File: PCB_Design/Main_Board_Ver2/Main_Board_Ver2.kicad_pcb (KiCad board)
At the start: 2 copper layers, 112.8 x 67.4 mm, 10 parts, among them J1 PJ-037A, J2 796949-4, J3 796949-4

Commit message: Making Changes to MAC variant
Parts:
- moved C5 0.14 mm to (188.2, 127.1)
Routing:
- net 12V: track 260.1 -> 186.9 mm
- net GND_Barrel: track 232.8 -> 171.8 mm, vias 2 -> 0
- net Uno_5V: track 70.6 -> 38.6 mm
- net GND_Uno: track 49.8 -> 24.0 mm
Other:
- net class Default removed

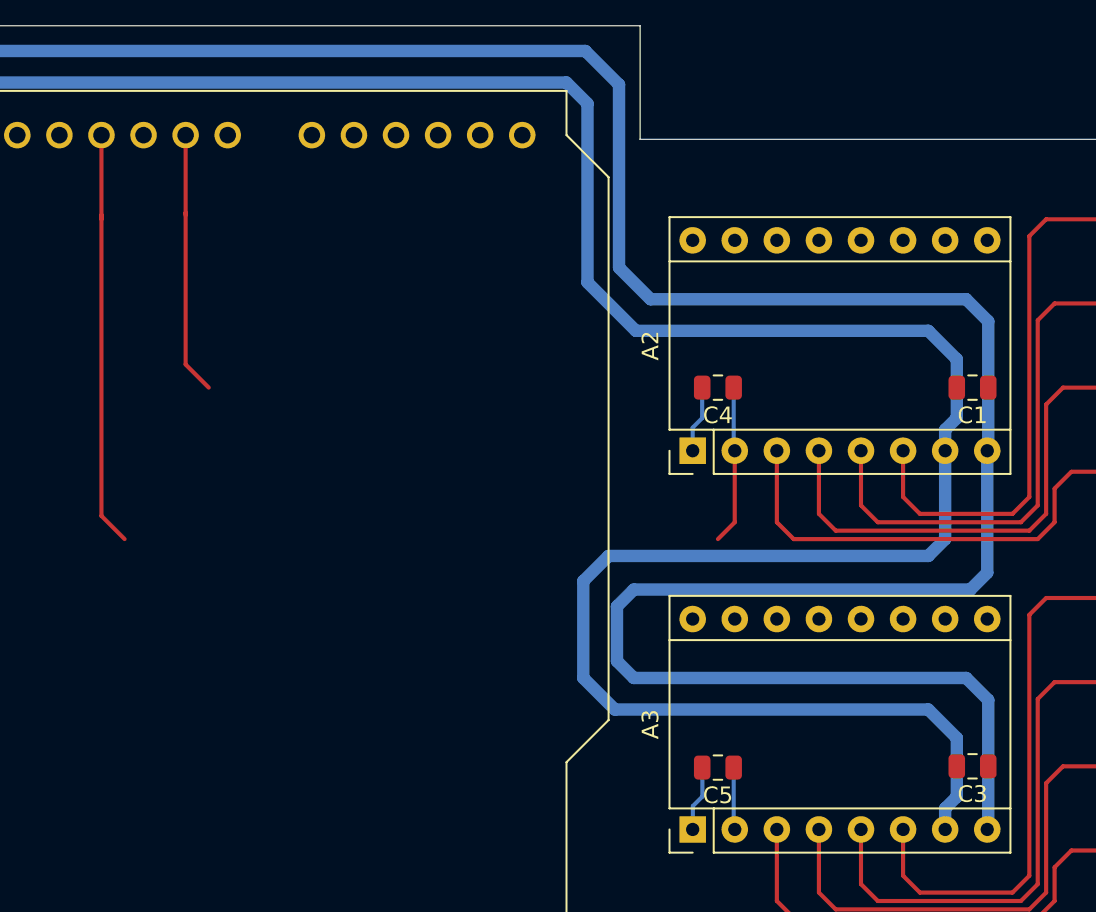
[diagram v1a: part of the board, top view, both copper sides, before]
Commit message: Finishing Power Lines
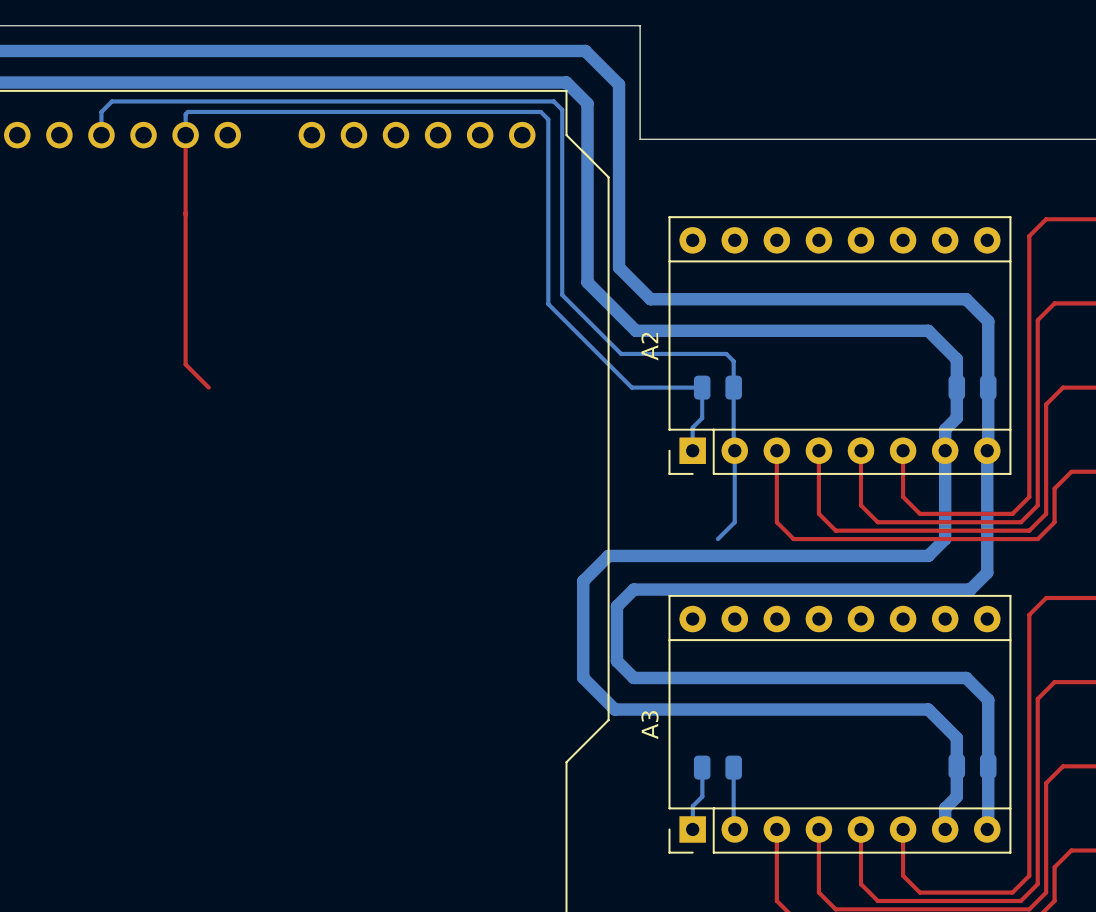
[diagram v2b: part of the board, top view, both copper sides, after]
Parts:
- C1, C3, C4, C5: moved to B.Cu
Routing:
- net GND_Uno: track 24.0 -> 70.0 mm
- net Uno_5V: track 38.6 -> 67.8 mm

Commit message: PCB Final
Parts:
- added REF**: MountingHole_3.2mm_M3_DIN965_Pad, MountingHole:MountingHole_3.2mm_M3_DIN965_Pad, F.Cu at (119.2, 68.5)
- added REF**: MountingHole_3.2mm_M3_DIN965_Pad, MountingHole:MountingHole_3.2mm_M3_DIN965_Pad, F.Cu at (119.2, 145.0)
- added REF**: MountingHole_3.2mm_M3_DIN965_Pad, MountingHole:MountingHole_3.2mm_M3_DIN965_Pad, F.Cu at (218.5, 141.0)
- added REF**: MountingHole_3.2mm_M3_DIN965_Pad, MountingHole:MountingHole_3.2mm_M3_DIN965_Pad, F.Cu at (218.5, 85.2)
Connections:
- A1 pad 1: Net-(A1-Pad1) -> unconnected-(A1-Pad1)
- A1 pad 10: Net-(A1-Pad10) -> unconnected-(A1-Pad10)
- A1 pad 11: Net-(A1-Pad11) -> unconnected-(A1-Pad11)
- A1 pad 12: Net-(A1-Pad12) -> unconnected-(A1-Pad12)
- A1 pad 13: Net-(A1-Pad13) -> unconnected-(A1-Pad13)
- A1 pad 14: Net-(A1-Pad14) -> unconnected-(A1-Pad14)
- A1 pad 15: Net-(A1-Pad15) -> unconnected-(A1-Pad15)
- A1 pad 16: Net-(A1-Pad16) -> unconnected-(A1-Pad16)
- A1 pad 2: Net-(A1-Pad2) -> unconnected-(A1-Pad2)
- A1 pad 21: Net-(A1-Pad21) -> unconnected-(A1-Pad21)
- A1 pad 22: Net-(A1-Pad22) -> unconnected-(A1-Pad22)
- A1 pad 23: Net-(A1-Pad23) -> unconnected-(A1-Pad23)
- A1 pad 24: Net-(A1-Pad24) -> unconnected-(A1-Pad24)
- A1 pad 25: Net-(A1-Pad25) -> unconnected-(A1-Pad25)
- A1 pad 26: Net-(A1-Pad26) -> unconnected-(A1-Pad26)
- A1 pad 27: Net-(A1-Pad27) -> unconnected-(A1-Pad27)
- A1 pad 28: Net-(A1-Pad28) -> unconnected-(A1-Pad28)
- A1 pad 29: Net-(A1-Pad29) -> unconnected-(A1-Pad29)
- A1 pad 3: Net-(A1-Pad3) -> unconnected-(A1-Pad3)
- A1 pad 30: Net-(A1-Pad30) -> unconnected-(A1-Pad30)
- A1 pad 31: Net-(A1-Pad31) -> unconnected-(A1-Pad31)
- A1 pad 32: Net-(A1-Pad32) -> unconnected-(A1-Pad32)
- A1 pad 4: Net-(A1-Pad4) -> unconnected-(A1-Pad4)
- A1 pad 6: Net-(A1-Pad6) -> unconnected-(A1-Pad6)
- A1 pad 8: Net-(A1-Pad8) -> unconnected-(A1-Pad8)
- A1 pad 9: Net-(A1-Pad9) -> unconnected-(A1-Pad9)
- A2 pad 10: Net-(A2-Pad10) -> unconnected-(A2-Pad10)
- A2 pad 11: Net-(A2-Pad11) -> unconnected-(A2-Pad11)
- A2 pad 12: Net-(A2-Pad12) -> unconnected-(A2-Pad12)
- A2 pad 15: D3 -> D4
- A2 pad 16: D2 -> D5
- A2 pad 9: Net-(A2-Pad9) -> unconnected-(A2-Pad9)
- A3 pad 10: Net-(A3-Pad10) -> unconnected-(A3-Pad10)
- A3 pad 11: Net-(A3-Pad11) -> unconnected-(A3-Pad11)
- A3 pad 12: Net-(A3-Pad12) -> unconnected-(A3-Pad12)
- A3 pad 15: D5 -> D2
- A3 pad 16: D4 -> D3
- A3 pad 9: Net-(A3-Pad9) -> unconnected-(A3-Pad9)
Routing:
- net D4: track 0.00 -> 64.6 mm
- net D5: track 0.00 -> 63.1 mm
- net D2: track 0.00 -> 36.3 mm
- net D3: track 0.00 -> 35.1 mm
- net Uno_5V: track 67.8 -> 98.7 mm
- net GND_Uno: track 70.0 -> 87.0 mm
- net Net-(A3-Pad13): track 0.00 -> 2.54 mm
- net Net-(A2-Pad13): track 0.00 -> 2.54 mm
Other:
- board size 112.8 x 67.4 mm -> 114.3 x 84.9 mm
